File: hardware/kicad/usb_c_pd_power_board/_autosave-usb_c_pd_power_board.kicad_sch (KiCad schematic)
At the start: 0 parts

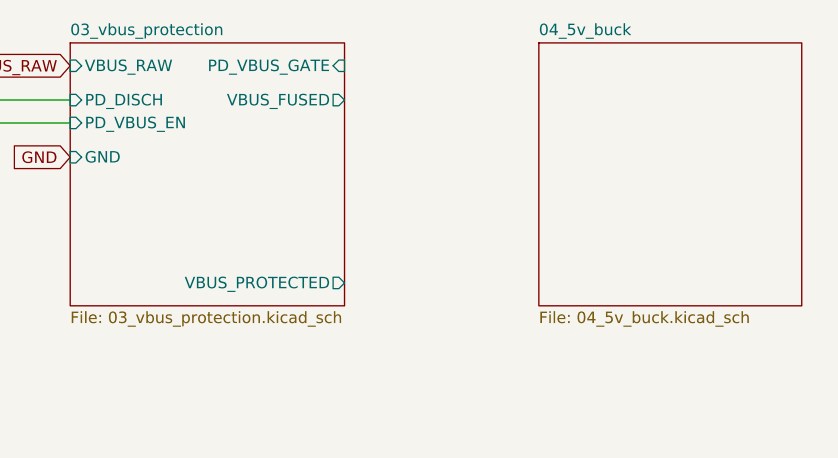
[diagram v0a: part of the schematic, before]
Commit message: Add USB-C PD input power and 5V buck schematic
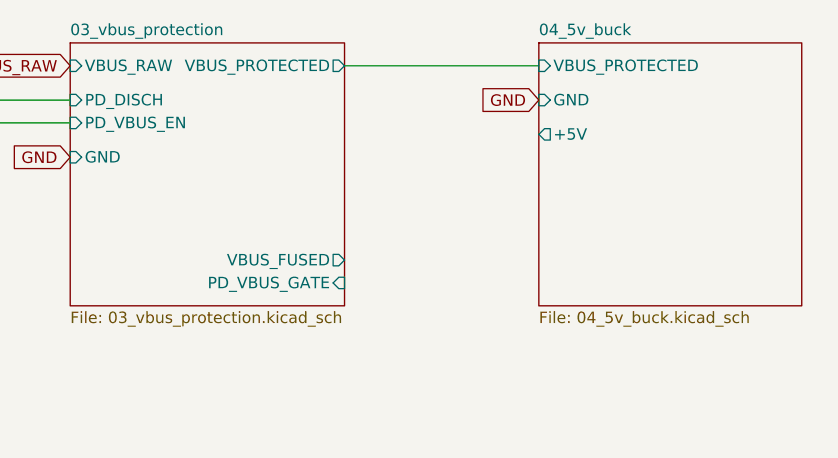
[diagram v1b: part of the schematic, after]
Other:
- sheet 04_5v_buck ports: added +5V, GND, VBUS_PROTECTED; removed none
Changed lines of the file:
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@@
+    (stroke (width 0) (type default))
+  )
+  (wire (pts (xy 180.34 26.67) (xy 201.93 26.67))
     (stroke (width 0) (type default))
   )
@@
     (property "Intersheetrefs" "${INTERSHEET_REFS}" (at 77.9757 38.1 0)
       (effects (font (size 1.27 1.27)) (justify left) hide)
+    )
+  )
+  (global_label "GND" (shape input) (at 201.93 30.48 180) (fields_autoplaced)
+    (effects (font (size 1.27 1.27)) (justify right))
+    (property "Intersheetrefs" "${INTERSHEET_REFS}" (at 195.0743 30.48 0)
+      (effects (font (size 1.27 1.27)) (justify right) hide)
     )
   )
@@
       (effects (font (size 1.27 1.27)) (justify left))
     )
-    (pin "VBUS_PROTECTED" output (at 180.34 50.8 0)
+    (pin "VBUS_PROTECTED" output (at 180.34 26.67 0)
       (effects (font (size 1.27 1.27)) (justify right))
     )
-    (pin "PD_VBUS_GATE" input (at 180.34 26.67 0)
+    (pin "PD_VBUS_GATE" input (at 180.34 50.8 0)
       (effects (font (size 1.27 1.27)) (justify right))
     )
-    (pin "VBUS_FUSED" output (at 180.34 30.48 0)
+    (pin "VBUS_FUSED" output (at 180.34 48.26 0)
       (effects (font (size 1.27 1.27)) (justify right))
     )
@@
       (effects (font (size 1.27 1.27)) (justify left top))
     )
+    (pin "VBUS_PROTECTED" input (at 201.93 26.67 180)
+      (effects (font (size 1.27 1.27)) (justify left))
+    )
+    (pin "GND" input (at 201.93 30.48 180)
+      (effects (font (size 1.27 1.27)) (justify left))
+    )
+    (pin "+5V" output (at 201.93 34.29 180)
+      (effects (font (size 1.27 1.27)) (justify left))
+    )
     (instances
